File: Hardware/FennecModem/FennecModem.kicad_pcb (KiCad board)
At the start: 2 copper layers, 75 x 116.7 mm, 43 parts, among them J201 Conn_Coaxial, SW101 RESET, U1 MCP6022, U201 DRA818V, U301 NCP1117-12_SOT223

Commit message: Bump fennec pcb
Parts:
- added C4: 1.6nF, Capacitor_SMD:C_0805_2012Metric, F.Cu at (155.3, 95.5)
- added C5: 1uF, Capacitor_SMD:C_0805_2012Metric, F.Cu at (152.8, 100.5)
- added JP1: Bypass Attenuation, Jumper:SolderJumper-2_P1.3mm_Open_TrianglePad1.0x1.5mm, F.Cu at (150.5, 92.5)
- added R6: 0R, Resistor_SMD:R_0805_2012Metric, F.Cu at (157.3, 97.5)
- added RV701: 10K, Potentiometer_SMD:Potentiometer_Bourns_TC33X_Vertical, F.Cu at (154.5, 92.5)
- C2: value 132nf -> 1.6nF; footprint Capacitor_THT:CP_Radial_D4.0mm_P2.00mm -> Capacitor_SMD:C_0805_2012Metric
- C3: value 72nf -> 360pF; footprint Capacitor_THT:CP_Radial_D4.0mm_P2.00mm -> Capacitor_SMD:C_0805_2012Metric
- R2: value 1k -> 99.4k; footprint Resistor_THT:R_Axial_DIN0207_L6.3mm_D2.5mm_P10.16mm_Horizontal -> Resistor_SMD:R_0805_2012Metric
- R3: value 10k -> 0R; footprint Resistor_THT:R_Axial_DIN0207_L6.3mm_D2.5mm_P10.16mm_Horizontal -> Resistor_SMD:R_0805_2012Metric
- R4: value 100R -> 151k; footprint Resistor_THT:R_Axial_DIN0207_L6.3mm_D2.5mm_P10.16mm_Horizontal -> Resistor_SMD:R_0805_2012Metric
- R5: value 1k -> 291k; footprint Resistor_THT:R_Axial_DIN0207_L6.3mm_D2.5mm_P10.16mm_Horizontal -> Resistor_SMD:R_0805_2012Metric
- moved R2 17.9 mm to (156.7, 108.5), turned to 90 degrees
- moved R3 16.7 mm to (153.8, 107.5), turned to 180 degrees
- moved U1 14.7 mm to (156.7, 102.5), turned to 90 degrees
- moved C3 10.4 mm to (160.8, 101.0)
- moved R5 6.59 mm to (151.6, 95.5), turned to 180 degrees
- moved R4 3.87 mm to (151.6, 97.5), turned to 0 degrees
- moved C2 2.04 mm to (159.7, 107.5), turned to 0 degrees
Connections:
- A1 pad 4: unconnected-(A1-GPIO2-Pad4) -> /TONE_OUT
- C2 pad 1: Net-(C2-Pad1) -> Net-(U1A-+)
- C2 pad 2: /Audio Processing/From MCU -> GND
- C3 pad 1: GND -> Net-(U1B-+)
- C3 pad 2: Net-(C3-Pad2) -> GND
- R2 pad 1: GND -> /TONE_OUT
- R2 pad 2: Net-(C2-Pad1) -> Net-(U1A-+)
- R3 pad 1: /Audio Processing/To Radio -> Net-(U1A--)
- R3 pad 2: Net-(C3-Pad2) -> Net-(R3-Pad2)
- R4 pad 1: GND -> Net-(R3-Pad2)
- R4 pad 2: /Audio Processing/To Radio -> Net-(C4-Pad1)
- R5 pad 1: Net-(C2-Pad1) -> Net-(C4-Pad1)
- R5 pad 2: Net-(C3-Pad2) -> Net-(U1B-+)
- U1 pad 1: unconnected-(U1-Pad1) -> Net-(R3-Pad2)
- U1 pad 2: unconnected-(U1A---Pad2) -> Net-(U1A--)
- U1 pad 3: unconnected-(U1A-+-Pad3) -> Net-(U1A-+)
- U1 pad 4: unconnected-(U1C-V--Pad4) -> GND
- U1 pad 5: unconnected-(U1B-+-Pad5) -> Net-(U1B-+)
- U1 pad 6: unconnected-(U1B---Pad6) -> Net-(U1B--)
- U1 pad 7: unconnected-(U1-Pad7) -> Net-(JP1-A)
- U1 pad 8: unconnected-(U1C-V+-Pad8) -> +3.3V
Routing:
- net /Audio Processing/To Radio: track 0.00 -> 22.3 mm
- net Net-(U1B-+): track 0.00 -> 15.2 mm, vias 0 -> 2
- net Net-(JP1-A): track 0.00 -> 12.9 mm
- net Net-(R3-Pad2): track 0.00 -> 12.6 mm
- net Net-(U1A-+): track 0.00 -> 4.87 mm
- net Net-(C4-Pad1): track 0.00 -> 3.83 mm
- net Net-(U1A--): track 0.00 -> 3.22 mm
- net Net-(U1B--): track 0.00 -> 2.86 mm
- net GND: vias 17 -> 18

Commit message: Route!
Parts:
- removed C1: 60nf, Capacitor_THT:CP_Radial_D4.0mm_P2.00mm
- removed C104: 100nf, Capacitor_SMD:C_0805_2012Metric
- removed C105: 1uf, Capacitor_SMD:C_0805_2012Metric
- removed D102: SCK, LED_SMD:LED_0805_2012Metric
- removed the G*** at (149.8, 125.7)
- removed R107: 330, Resistor_SMD:R_0805_2012Metric
- removed SW101: RESET, Button_Switch_THT:SW_PUSH_6mm_H5mm
- added C6: 110nf, Capacitor_SMD:C_0805_2012Metric, F.Cu at (147.1, 126.2)
- added JP2: SolderJumper_2_Open, Jumper:SolderJumper-2_P1.3mm_Open_TrianglePad1.0x1.5mm, B.Cu at (142.2, 146.8)
- added JP3: SolderJumper_2_Open, Jumper:SolderJumper-2_P1.3mm_Open_TrianglePad1.0x1.5mm, B.Cu at (146.1, 146.8)
- added JP4: SolderJumper_2_Open, Jumper:SolderJumper-2_P1.3mm_Open_TrianglePad1.0x1.5mm, B.Cu at (149.9, 146.8)
- added JP5: SolderJumper_2_Open, Jumper:SolderJumper-2_P1.3mm_Open_TrianglePad1.0x1.5mm, B.Cu at (154.3, 146.8)
- added JP6: SolderJumper_2_Open, Jumper:SolderJumper-2_P1.3mm_Open_TrianglePad1.0x1.5mm, B.Cu at (158.1, 146.8)
- added R7: 0R, Resistor_SMD:R_0805_2012Metric, F.Cu at (158.1, 124.5)
- added R8: 100k, Resistor_SMD:R_0805_2012Metric, F.Cu at (149.2, 123.8)
- added RV1: 10K, Potentiometer_SMD:Potentiometer_Bourns_TC33X_Vertical, F.Cu at (153.0, 125.7)
- added TP1: SleepTP, TestPoint:TestPoint_Bridge_Pitch2.0mm_Drill0.7mm, F.Cu at (159.3, 92.4)
- added TP2: H/L, TestPoint:TestPoint_Bridge_Pitch2.0mm_Drill0.7mm, F.Cu at (149.1, 92.5)
- added TP3: PTT, TestPoint:TestPoint_Bridge_Pitch2.0mm_Drill0.7mm, F.Cu at (156.7, 92.4)
- added TP4: AudioOut, TestPoint:TestPoint_Bridge_Pitch2.0mm_Drill0.7mm, F.Cu at (171.4, 92.4)
- added TP5: AudioIn, TestPoint:TestPoint_Bridge_Pitch2.0mm_Drill0.7mm, F.Cu at (151.6, 92.4)
- added TP6: SQL, TestPoint:TestPoint_Bridge_Pitch2.0mm_Drill0.7mm, F.Cu at (154.2, 90.4)
- added TP7: TXD, TestPoint:TestPoint_Bridge_Pitch2.0mm_Drill0.7mm, F.Cu at (168.9, 92.4)
- added TP8: RXD, TestPoint:TestPoint_Bridge_Pitch2.0mm_Drill0.7mm, F.Cu at (166.4, 92.4)
- A1: footprint Module:RaspberryPi_Pico_Common_Unspecified -> Module:RaspberryPi_Pico_Common_THT
- G***: moved to B.Cu
- R1: value 10k -> 100k; footprint Resistor_THT:R_Axial_DIN0207_L6.3mm_D2.5mm_P10.16mm_Horizontal -> Resistor_SMD:R_0805_2012Metric
- moved R201 76.5 mm to (148.6, 47.2), turned to -90 degrees
- moved R206 33.1 mm to (156.7, 98.1)
- moved R1 32.7 mm to (149.4, 127.3), turned to -90 degrees
- moved C201 31.0 mm to (199.0, 103.2)
- moved C202 31.0 mm to (199.0, 106.2)
- moved A1 25.8 mm to (121.9, 41.9)
- moved R204 23.9 mm to (199.0, 112.2), turned to 0 degrees
- moved R203 22.3 mm to (199.0, 109.2), turned to 0 degrees
- moved C3 21.7 mm to (148.2, 118.7), turned to 180 degrees
- moved C2 20.7 mm to (141.7, 117.6), turned to -90 degrees
- moved RV701 20.1 mm to (156.7, 112.4), turned to 90 degrees
- moved R6 18.6 mm to (151.7, 115.2), turned to 90 degrees
- moved R108 18.0 mm to (162.6, 47.2), turned to -90 degrees
- moved C4 17.8 mm to (153.7, 113.2), turned to -90 degrees
- moved R2 17.2 mm to (140.7, 114.6), turned to 0 degrees
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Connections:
- A1 pad 11: unconnected-(A1-GPIO8-Pad11) -> /RXD
- A1 pad 12: unconnected-(A1-GPIO9-Pad12) -> /TXD
- A1 pad 13: Net-(A1-GND-Pad13) -> GND
- A1 pad 14: unconnected-(A1-GPIO10-Pad14) -> /PTT
- A1 pad 15: unconnected-(A1-GPIO11-Pad15) -> /Sleep
- A1 pad 16: unconnected-(A1-GPIO12-Pad16) -> /H/L
- A1 pad 17: unconnected-(A1-GPIO13-Pad17) -> /SQL
- A1 pad 18: Net-(A1-GND-Pad13) -> GND
- A1 pad 21: unconnected-(A1-GPIO16-Pad21) -> /SDO
- A1 pad 22: unconnected-(A1-GPIO17-Pad22) -> /CARD_SEL
- A1 pad 23: Net-(A1-GND-Pad13) -> GND
- A1 pad 24: unconnected-(A1-GPIO18-Pad24) -> /SPI_CLK
- A1 pad 25: unconnected-(A1-GPIO19-Pad25) -> /SDI
- A1 pad 26: unconnected-(A1-GPIO20-Pad26) -> Net-(A1-GPIO20)
- A1 pad 27: unconnected-(A1-GPIO21-Pad27) -> Net-(A1-GPIO21)
- A1 pad 28: Net-(A1-GND-Pad13) -> GND
- A1 pad 29: unconnected-(A1-GPIO22-Pad29) -> Net-(A1-GPIO22)
- A1 pad 3: Net-(A1-GND-Pad13) -> GND
- A1 pad 31: unconnected-(A1-GPIO26_ADC0-Pad31) -> /TONE_IN
- A1 pad 33: unconnected-(A1-AGND-Pad33) -> GNDA
- A1 pad 36: unconnected-(A1-3V3-Pad36) -> +3.3V
- A1 pad 38: Net-(A1-GND-Pad13) -> GND
- A1 pad 39: unconnected-(A1-VSYS-Pad39) -> +5V
- A1 pad 6: unconnected-(A1-GPIO4-Pad6) -> Net-(A1-GPIO4)
- A1 pad 7: unconnected-(A1-GPIO5-Pad7) -> Net-(A1-GPIO5)
- A1 pad 8: Net-(A1-GND-Pad13) -> GND
- A1 pad 9: unconnected-(A1-GPIO6-Pad9) -> /STAT
- D101 pad 1: /STAT -> GND
- D201 pad 1: /Radio/SQL -> /SQL
- D203 pad 1: /Radio/PTT -> /PTT
- R1 pad 1: /Audio Processing/To MCU -> /TONE_IN
- R1 pad 2: /Audio Processing/From Radio -> +3.3V
- R103 pad 2: +5V -> /STAT
- R108 pad 2: +5V -> +3.3V
- R201 pad 1: /Radio/Sleep -> /Sleep
- R201 pad 2: +5V -> +3.3V
- R202 pad 2: +5V -> +3.3V
- R203 pad 2: +5V -> +3.3V
- R204 pad 2: +5V -> +3.3V
- R205 pad 2: +5V -> +3.3V
- R206 pad 1: /Radio/PTT -> /PTT
- U201 pad 1: /Radio/SQL -> /SQL
- U201 pad 6: /Radio/Sleep -> /Sleep
- U201 pad 7: /Radio/H/L -> /H/L
- U302 pad 11: /Backplane/I2C_SCL -> /SCL
- U302 pad 12: /Backplane/SPI_CLK -> /SPI_CLK
- U302 pad 13: /Backplane/I2C_SDA -> /SDA
- U302 pad 14: /Backplane/SPI_SDA1 -> /SDI
- U302 pad 16: /Backplane/SPI_SDA2 -> /SPI2
- U302 pad 17: unconnected-(U302-SPI_SD0-Pad17) -> /SDO
- U302 pad 18: /Backplane/SPI_SDA3 -> /SPI3
- U302 pad 20: /Backplane/SPI_SDA4 -> /SPI4
- U302 pad 4: /Backplane/CARD_SEL -> /CARD_SEL
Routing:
- net +5V: track 0.00 -> 138.2 mm, vias 0 -> 1
- net Net-(A1-GPIO22): track 0.00 -> 103.1 mm, vias 0 -> 1
- net +3.3V: track 0.00 -> 102.5 mm, vias 0 -> 2
- net GNDA: track 0.00 -> 95.3 mm, vias 0 -> 2
- net Net-(A1-GPIO21): track 0.00 -> 91.2 mm, vias 0 -> 1
- net /TONE_IN: track 0.00 -> 83.1 mm, vias 0 -> 2
- net Net-(A1-GPIO20): track 0.00 -> 82.2 mm, vias 0 -> 1
- net /SDI: track 0.00 -> 81.8 mm, vias 0 -> 1
- net /SPI_CLK: track 0.00 -> 78.7 mm, vias 0 -> 1
- net /CARD_SEL: track 0.00 -> 74.1 mm, vias 0 -> 1
- net /SDO: track 0.00 -> 72.9 mm
- net /PTT: track 0.00 -> 61.4 mm, vias 0 -> 1
- net /STAT: track 0.00 -> 53.1 mm, vias 0 -> 2
- net /Sleep: track 0.00 -> 50.7 mm, vias 0 -> 2
- net /SQL: track 0.00 -> 50.6 mm, vias 0 -> 1
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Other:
- board text added: "AFSK In"
- board text added: "AFSK Out"

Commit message: Add stackup and fan
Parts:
- added M1: Fan, Connector_PinHeader_2.54mm:PinHeader_1x02_P2.54mm_Vertical, F.Cu at (142.5, 95.7)
- added Q1: 2N3906, Package_TO_SOT_THT:TO-92_Inline, F.Cu at (141.5, 100.0)
- added R9: 10k, Resistor_SMD:R_0805_2012Metric, F.Cu at (138.0, 100.5)
- moved REF** 24.5 mm to (179.0, 89.5)
- moved G*** 4.30 mm to (181.2, 79.0)
- moved REF** 4.30 mm to (179.5, 66.0)
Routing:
- net +3.3V: track 102.5 -> 21.8 mm
- added copper zone on In2.Cu, net +3.3V
- added copper zone on In1.Cu, net GND
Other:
- copper layers 2 -> 4
- board text added: "Optional Fan"

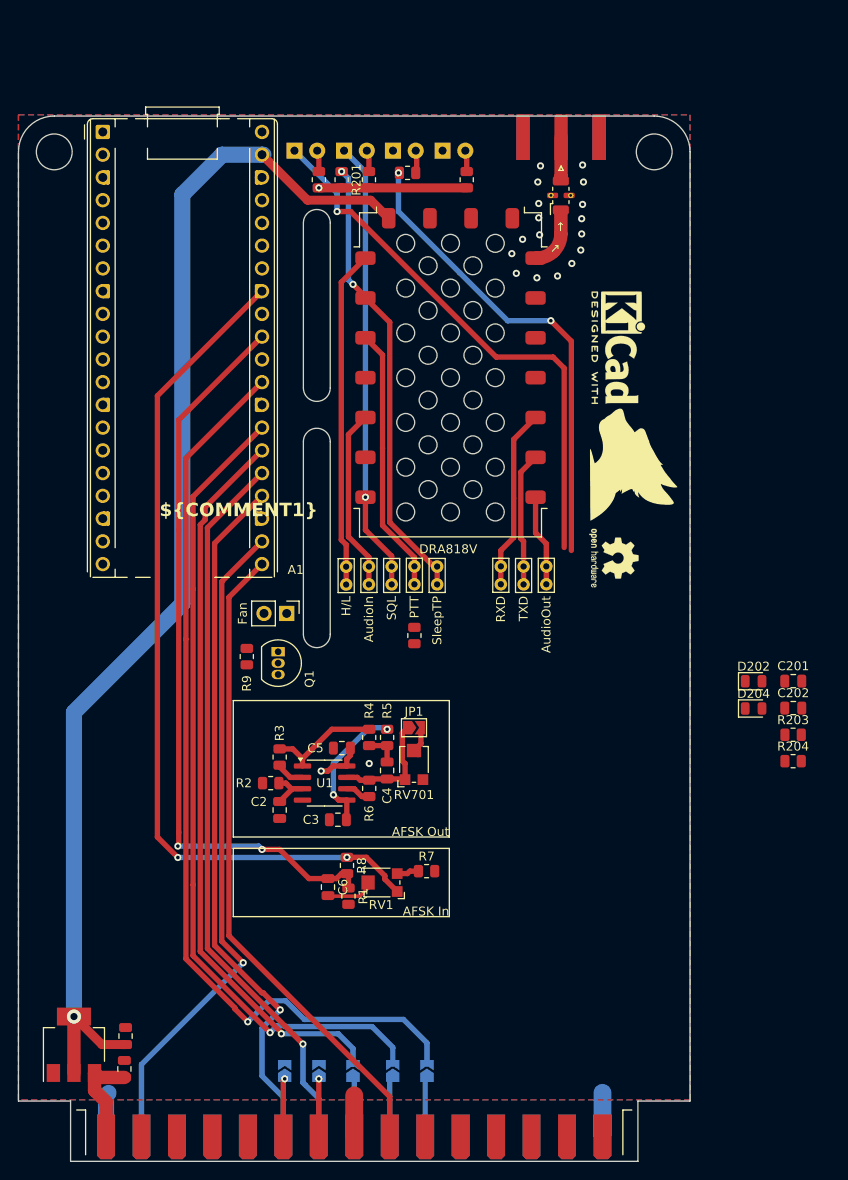
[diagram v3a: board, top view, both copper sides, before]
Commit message: Change all power switching
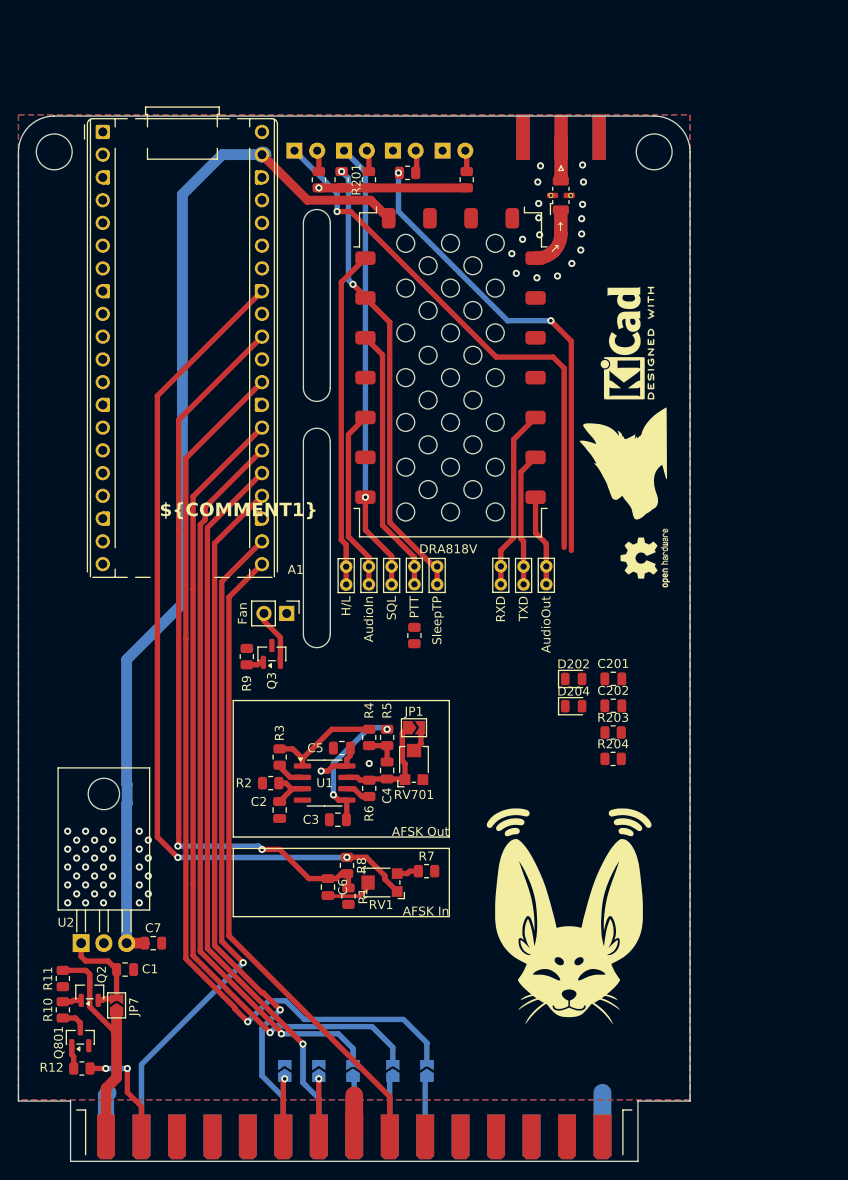
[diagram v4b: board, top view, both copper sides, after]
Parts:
- removed C302: 1μf, Capacitor_SMD:C_0805_2012Metric
- removed C303: 0.1μf, Capacitor_SMD:C_0805_2012Metric
- removed Q1: 2N3906, Package_TO_SOT_THT:TO-92_Inline
- removed U301: NCP1117-12_SOT223, Package_TO_SOT_SMD:SOT-223-3_TabPin2
- added C1: 10μf, Capacitor_SMD:C_0805_2012Metric, F.Cu at (124.4, 135.4)
- added C7: 0.1μf, Capacitor_SMD:C_0805_2012Metric, F.Cu at (127.5, 132.5)
- added JP7: SolderJumper_2_Open, Jumper:SolderJumper-2_P1.3mm_Open_TrianglePad1.0x1.5mm, F.Cu at (123.5, 139.4)
- added Q2: AO3401A, Package_TO_SOT_SMD:SOT-23, F.Cu at (120.5, 137.9)
- added Q3: MMBT3906, Package_TO_SOT_SMD:SOT-23, F.Cu at (140.8, 100.2)
- added Q801: MMBT3904, Package_TO_SOT_SMD:SOT-23, F.Cu at (119.4, 143.0)
- added R10: 1K, Resistor_SMD:R_0805_2012Metric, F.Cu at (117.5, 139.9)
- added R11: 100K, Resistor_SMD:R_0805_2012Metric, F.Cu at (117.5, 136.4)
- added R12: 1K, Resistor_SMD:R_0805_2012Metric, F.Cu at (119.6, 146.5)
- added U2: L7805, Package_TO_SOT_THT:TO-220-3_Horizontal_TabDown, F.Cu at (119.5, 132.5)
- G***: moved to F.Cu
- moved G*** 24.9 mm to (174.0, 128.7), turned to 0 degrees
- moved C201 20.1 mm to (178.9, 103.0)
- moved C202 20.1 mm to (178.9, 106.0)
- moved D202 20.1 mm to (174.5, 103.0)
- moved D204 20.1 mm to (174.5, 106.0)
- moved R203 20.1 mm to (178.9, 109.0)
- moved R204 20.1 mm to (178.9, 111.9)
- moved REF** 3.50 mm to (182.5, 89.5), turned to 90 degrees
- moved G*** 1.25 mm to (180.0, 79.0), turned to 90 degrees
- moved REF** 1.12 mm to (180.5, 65.5), turned to 90 degrees
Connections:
- A1 pad 34: unconnected-(A1-GPIO28_ADC2-Pad34) -> /FAN
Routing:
- net +5V: track 138.2 -> 116.2 mm, vias 1 -> 0
- net +12V: track 11.2 -> 25.5 mm
- net /Backplane/CARD_EN: track 0.00 -> 12.4 mm, vias 0 -> 2
- net Net-(JP7-B): track 0.00 -> 11.4 mm
- net Net-(M1--): track 0.00 -> 6.22 mm
- net Net-(Q801-C): track 0.00 -> 2.84 mm
- net Net-(Q801-B): track 0.00 -> 2.64 mm
- net Net-(Q2-G): track 0.00 -> 2.11 mm
- net Net-(Q3-B): track 0.00 -> 1.96 mm
- net GND: vias 18 -> 54
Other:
- board text added: "- Blunt, Freefall by Mark Stanley"
- board text added: "Sir, I beleive if you look past the obvious answer, you'll find one that is even more obvious."
- board text added: "With Thanks To: KA2QFX Arthur A. SNHU RhainBowMetall Handiko squirrelengineering.com And my community beta testers"

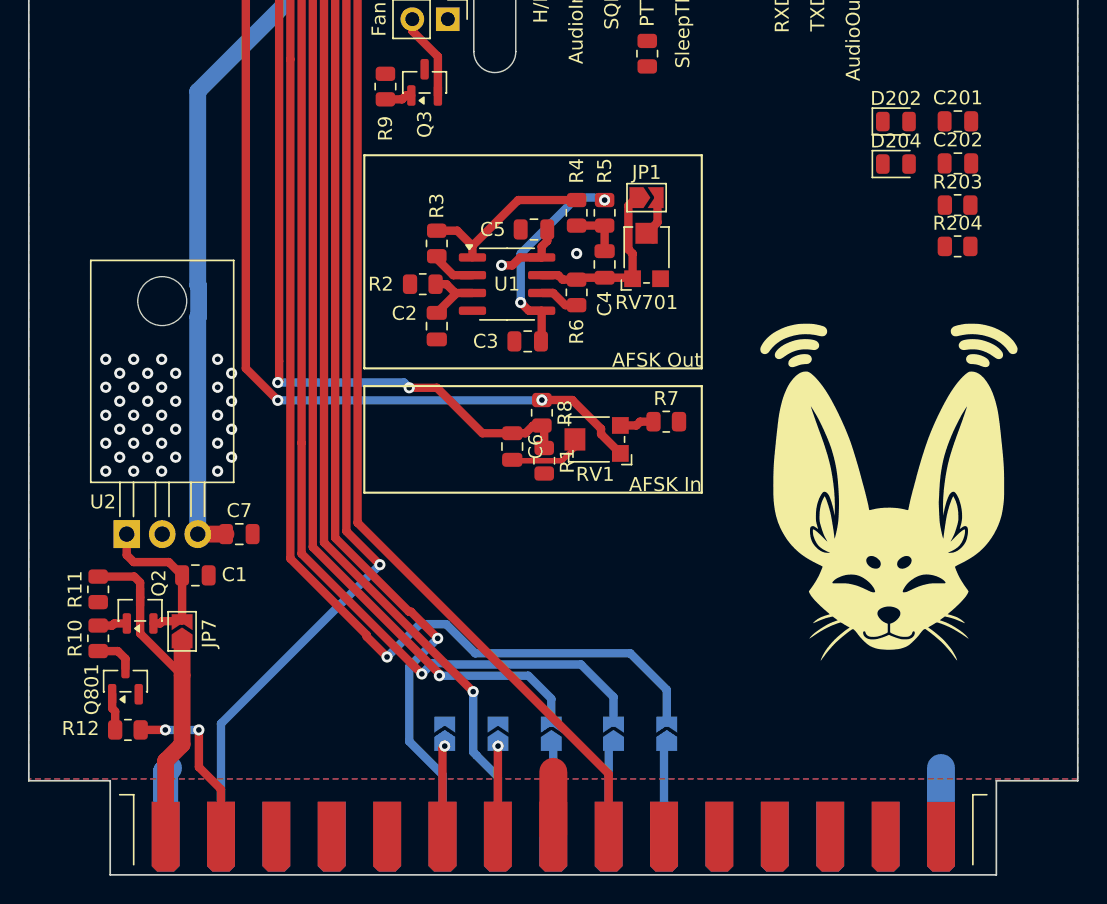
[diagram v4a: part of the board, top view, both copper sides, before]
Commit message: add jumpers and bump kicad libs
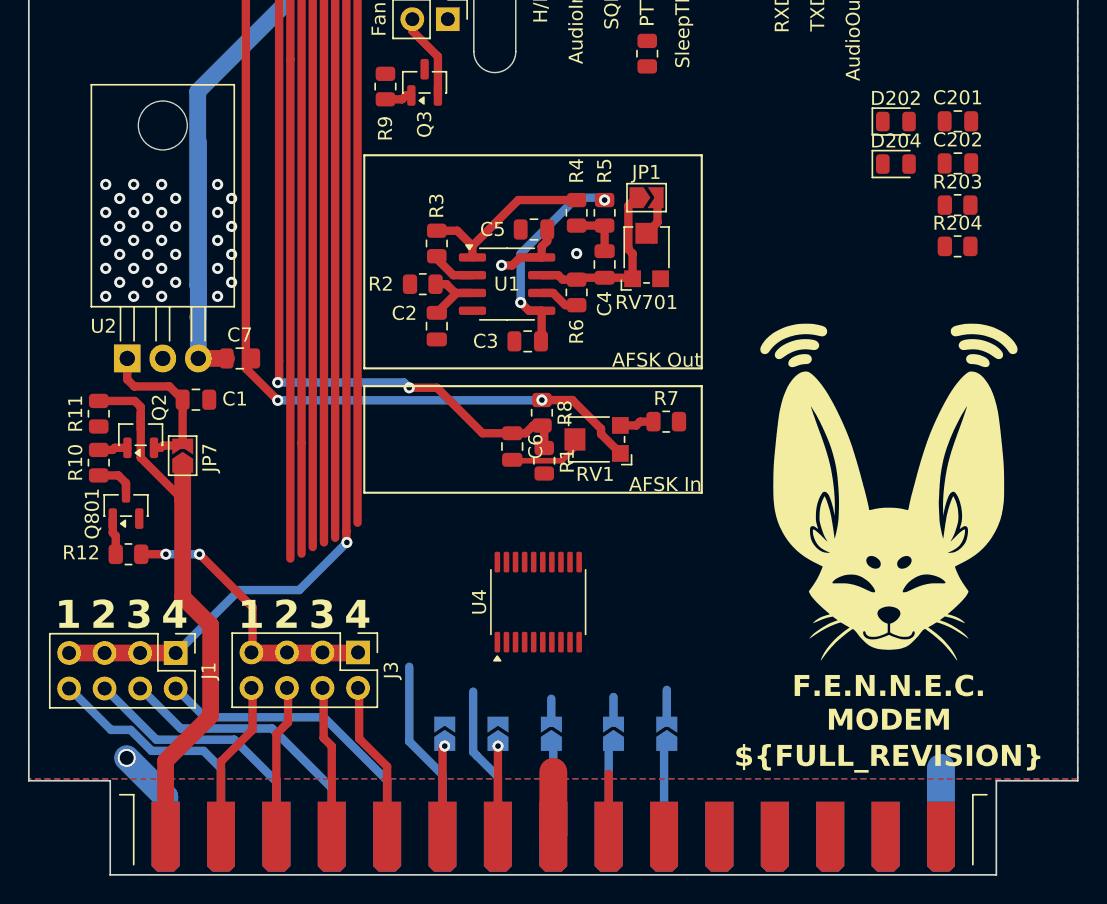
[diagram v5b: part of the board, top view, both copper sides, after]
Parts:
- added J1: Conn_02x04_Odd_Even, Connector_PinHeader_2.54mm:PinHeader_2x04_P2.54mm_Vertical, F.Cu at (123.0, 141.0)
- added J3: Conn_02x04_Odd_Even, Connector_PinHeader_2.54mm:PinHeader_2x04_P2.54mm_Vertical, F.Cu at (136.0, 141.0)
- added U4: SN74LVC245APW, Package_SO:TSSOP-20_4.4x6.5mm_P0.65mm, F.Cu at (148.9, 137.4)
- moved C7 12.6 mm to (127.6, 119.9)
- moved R12 12.6 mm to (119.6, 133.9)
- moved U2 12.6 mm to (119.5, 119.9)
- moved C1 12.6 mm to (124.5, 122.9)
- moved JP7 12.6 mm to (123.5, 126.9)
- moved Q2 12.6 mm to (120.5, 125.4)
- moved R10 12.6 mm to (117.5, 127.4)
- moved R11 12.6 mm to (117.5, 123.9)
- moved Q801 12.6 mm to (119.5, 130.5)
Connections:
- U302 pad 10: unconnected-(U302-CARD_SEL4-Pad10) -> Net-(J1-Pin_2)
- U302 pad 3: /Backplane/CARD_EN -> Net-(J3-Pin_8)
- U302 pad 4: /CARD_SEL -> Net-(J1-Pin_8)
- U302 pad 5: unconnected-(U302-CARD_EN2-Pad5) -> Net-(J3-Pin_6)
- U302 pad 6: unconnected-(U302-CARD_SEL2-Pad6) -> Net-(J1-Pin_6)
- U302 pad 7: unconnected-(U302-CARD_EN3-Pad7) -> Net-(J3-Pin_4)
- U302 pad 8: unconnected-(U302-CARD_SEL3-Pad8) -> Net-(J1-Pin_4)
- U302 pad 9: unconnected-(U302-CARD_EN4-Pad9) -> Net-(J3-Pin_2)
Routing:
- net Net-(A1-GPIO22): track 103.1 -> 70.3 mm, vias 1 -> 0
- net Net-(A1-GPIO21): track 91.2 -> 64.0 mm, vias 1 -> 0
- net /SDO: track 72.9 -> 47.5 mm
- net Net-(J1-Pin_2): track 0.00 -> 21.8 mm
- net Net-(A1-GPIO20): track 82.2 -> 60.6 mm, vias 1 -> 0
- net Net-(J1-Pin_4): track 0.00 -> 20.1 mm
- net Net-(J1-Pin_6): track 0.00 -> 18.9 mm
- net Net-(J1-Pin_8): track 0.00 -> 18.1 mm
- net /SDI: track 81.8 -> 66.7 mm, vias 1 -> 0
- net +12V: track 25.5 -> 39.7 mm
- net /SPI_CLK: track 78.7 -> 65.5 mm, vias 1 -> 0
- net Net-(J3-Pin_8): track 0.00 -> 11.5 mm
- net Net-(J3-Pin_2): track 0.00 -> 11.4 mm
- net Net-(J3-Pin_6): track 0.00 -> 10.9 mm
- net Net-(J3-Pin_4): track 0.00 -> 10.8 mm
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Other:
- board text added: "1"
- board text added: "2"
- board text added: "3"
- board text added: "4"
